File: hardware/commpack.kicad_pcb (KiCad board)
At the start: 2 copper layers, 103.8 x 62.5 mm, 15 parts, among them J1 1240COMM, J2 1240COMM_EXT, J3 L8BE-1G1T-91A, J4 USB_B, U3 27C128

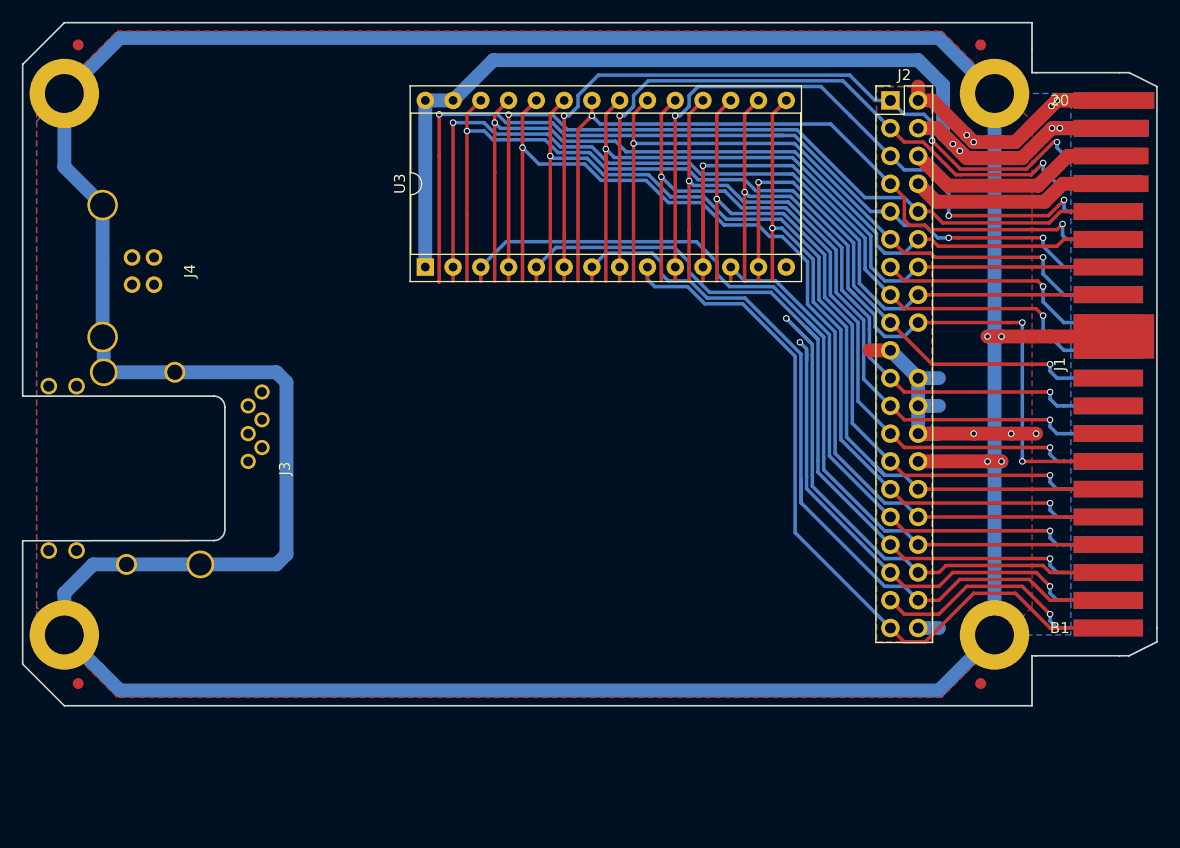
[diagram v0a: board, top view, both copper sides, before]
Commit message: Add Omega2 footprint to board.
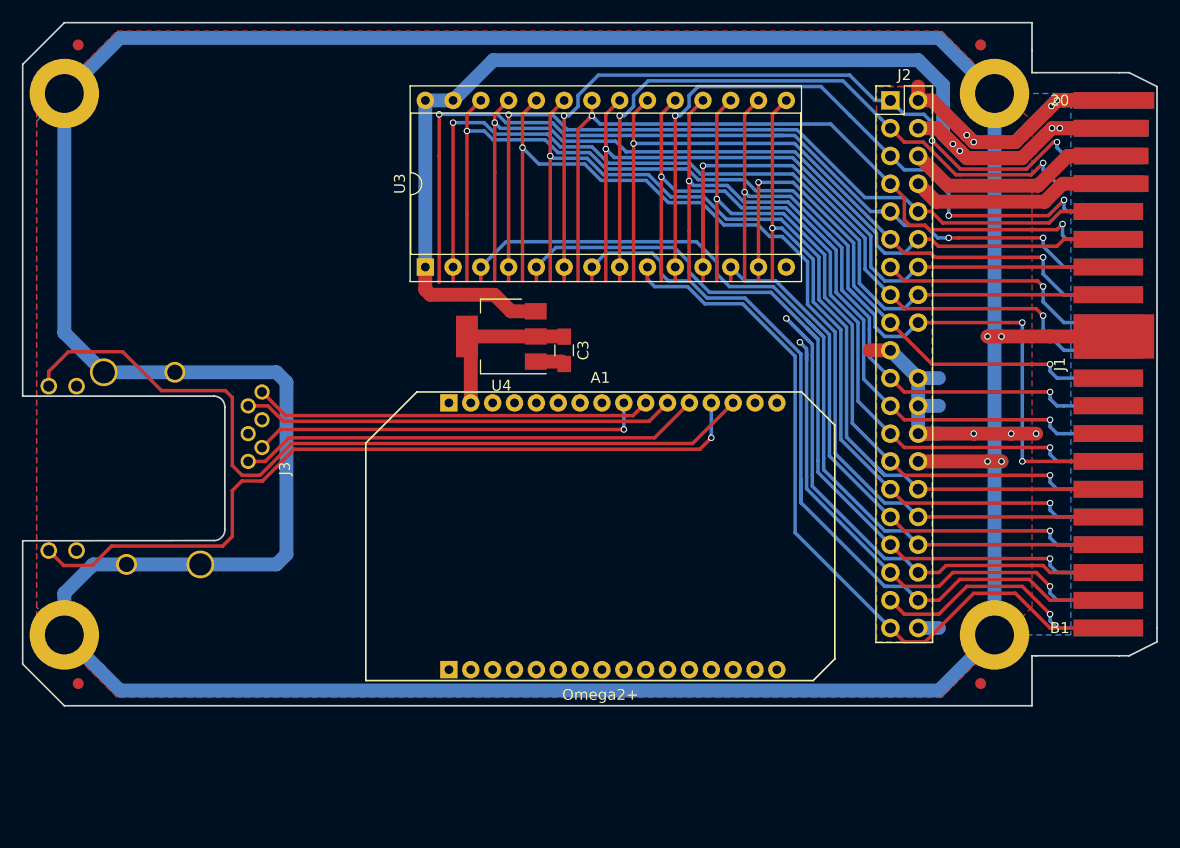
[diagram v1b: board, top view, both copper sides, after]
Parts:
- removed J4: USB_B, USB-B
- added A1: Omega2+, Omega2, F.Cu at (174.8, 104.6)
- added C3: 22u, Capacitors_SMD:C_0805_HandSoldering, F.Cu at (171.4, 87.6)
- added U4: AP1117-33, TO_SOT_Packages_SMD:SOT-223-3_TabPin2, F.Cu at (165.7, 86.4)
- moved Bonsai 16.6 mm to (186.7, 105.4)
- moved G*** 16.3 mm to (172.7, 104.1)
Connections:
- J3 pad 13: Net-(J3-Pad13) -> GND
- J3 pad 15: Net-(J3-Pad15) -> GND
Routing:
- net Net-(A1-PadB14): track 0.00 -> 75.8 mm
- net Net-(A1-PadB13): track 0.00 -> 71.7 mm, vias 0 -> 1
- net Net-(A1-PadB12): track 0.00 -> 42.6 mm
- net Net-(A1-PadB11): track 0.00 -> 39.6 mm
- net Net-(A1-PadB10): track 0.00 -> 36.5 mm
- net Net-(A1-PadB9): track 0.00 -> 36.2 mm, vias 0 -> 1
- net +3V3: track 0.00 -> 15.1 mm
- net +5V: track 96.2 -> 109.2 mm
- net GND: track 53.5 -> 56.2 mm

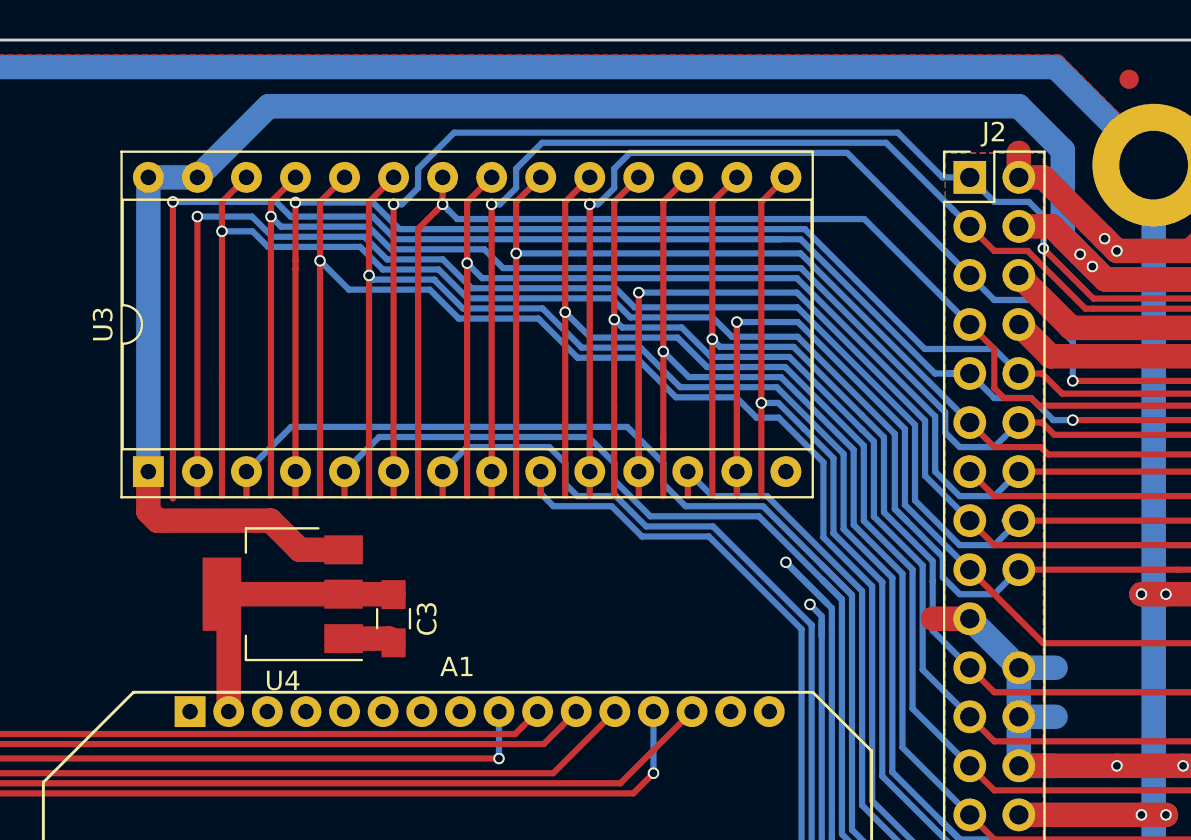
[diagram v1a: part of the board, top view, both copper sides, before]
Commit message: Reroute traces under 27C128 socket again.
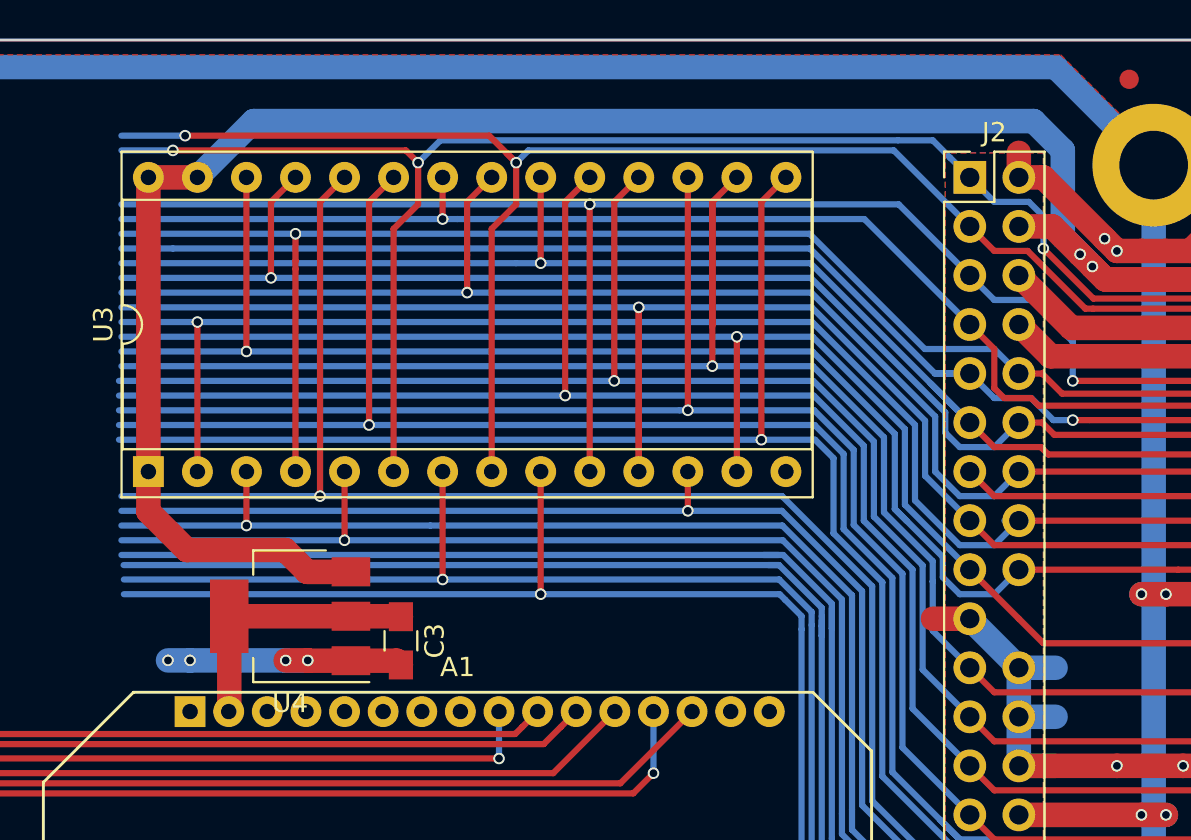
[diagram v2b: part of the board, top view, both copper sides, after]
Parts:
- moved C3 1.20 mm to (171.8, 88.8)
- moved U4 1.20 mm to (166.1, 87.5)
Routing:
- net /H-RST: track 44.5 -> 81.8 mm, vias 2 -> 1
- net /H-~CS: track 47.1 -> 80.6 mm, vias 1 -> 0
- net /H-D4: track 60.0 -> 89.6 mm
- net /H-D3: track 64.1 -> 93.6 mm
- net /H-D2: track 47.9 -> 77.5 mm
- net /H-D1: track 50.0 -> 79.3 mm, vias 1 -> 2
- net /H-D0: track 62.1 -> 86.6 mm
- net /H-A1: track 67.7 -> 91.5 mm, vias 0 -> 1
- net /H-D5: track 68.6 -> 90.6 mm
- net /H-A0: track 61.0 -> 81.2 mm
- net /H-A2: track 64.1 -> 83.8 mm, vias 2 -> 3
- net /H-D6: track 67.6 -> 86.0 mm
- net /H-A3: track 71.3 -> 88.5 mm, vias 0 -> 1
- net /H-D7: track 72.4 -> 88.5 mm
- net /H-INT: track 81.9 -> 67.9 mm, vias 3 -> 2
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
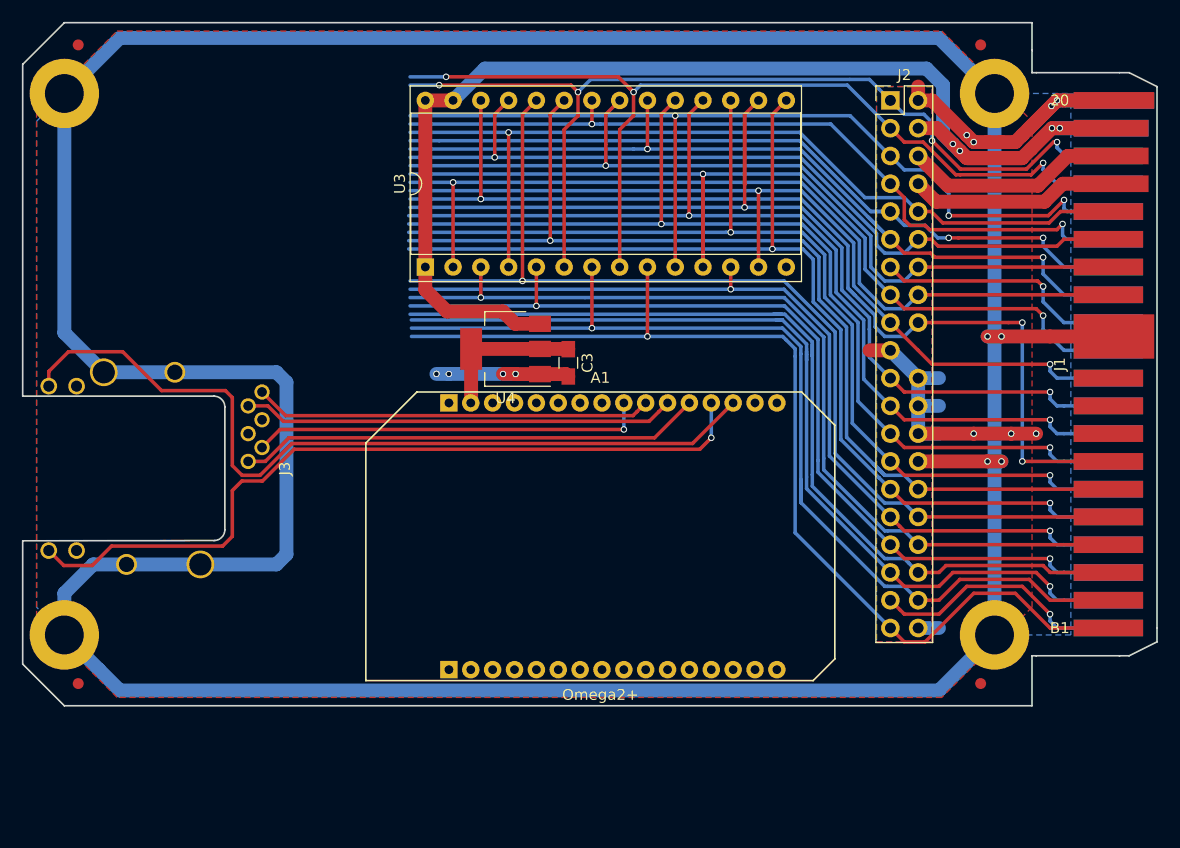
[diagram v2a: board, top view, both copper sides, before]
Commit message: Change ATA pinout, rip up EPROM socket and Omega2.
I missed two grounded pins when I did the original ATA connector pinout,
so this drops the +12V and -12V connections and rearranges everything to
avoid shorting two of the address lines to ground.
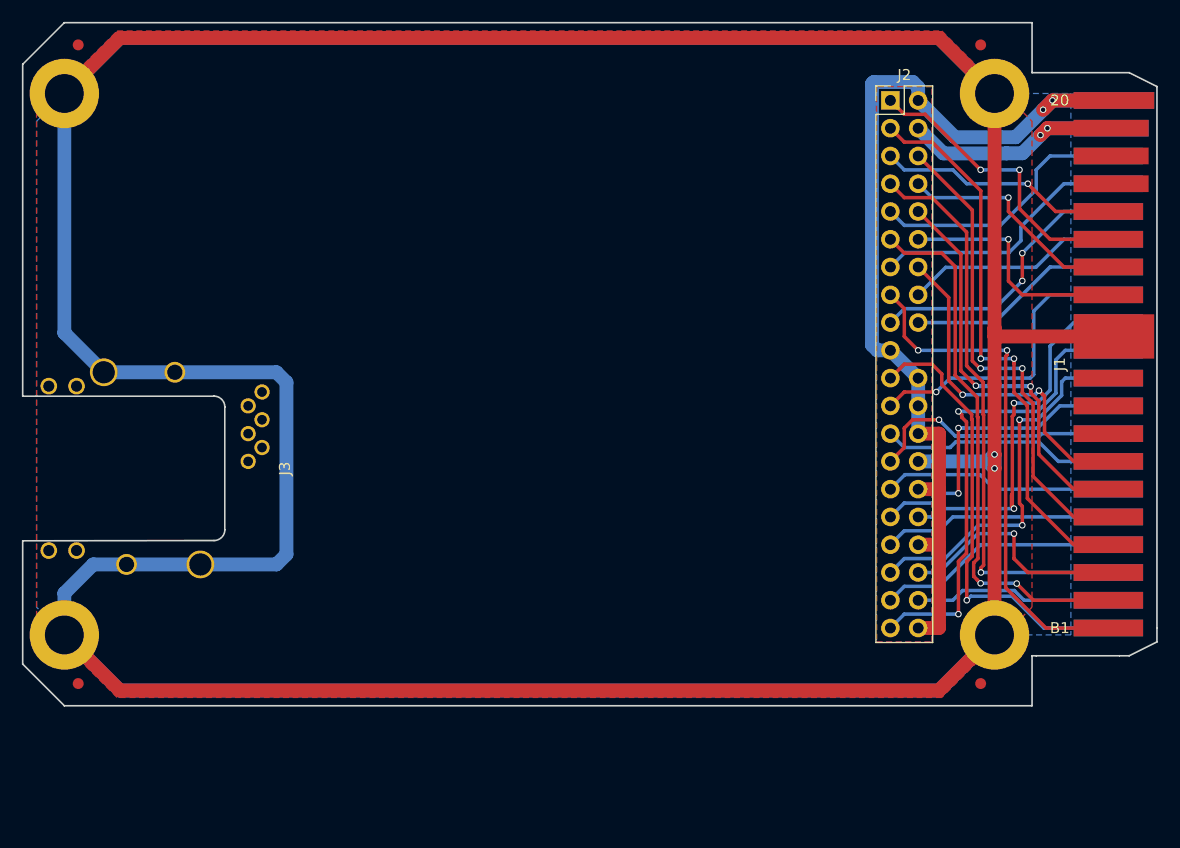
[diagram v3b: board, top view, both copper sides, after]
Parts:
- removed A1: Omega2+, Omega2
- removed Bonsai: Bonsai, ether1240:Bonsai
- removed C3: 22u, Capacitors_SMD:C_0805_HandSoldering
- removed G***: LOGO, ether1240:OSHW
- removed U3: 27C128, Housings_DIP:DIP-28_W15.24mm_Socket
- removed U4: AP1117-33, TO_SOT_Packages_SMD:SOT-223-3_TabPin2
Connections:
- J1 pad B17: +12VA -> Net-(J1-PadB17)
- J1 pad B18: -12VA -> Net-(J1-PadB18)
- J2 pad 1: /H-A4 -> /H-A8
- J2 pad 10: /H-A6 -> /H-A11
- J2 pad 11: /H-~RS -> /H-A3
- J2 pad 12: /H-A8 -> /H-A12
- J2 pad 13: Net-(J1-PadA12) -> /H-A2
- J2 pad 14: /H-A10 -> /H-A13
- J2 pad 15: /H-D0 -> /H-A1
- J2 pad 16: /H-A12 -> /H-~RD
- J2 pad 17: /H-D2 -> /H-A0
- J2 pad 18: /H-A13 -> /H-INT
- J2 pad 21: /H-D4 -> /H-~WR
- J2 pad 23: /H-D6 -> /H-~RS
- J2 pad 27: /H-D5 -> /H-D6
- J2 pad 29: /H-D3 -> /H-D5
- J2 pad 3: /H-A2 -> /H-A7
- J2 pad 30: /H-A11 -> GND
- J2 pad 31: /H-D1 -> /H-D4
- J2 pad 32: /H-A9 -> Net-(J1-PadA12)
- J2 pad 33: /H-A5 -> /H-D3
- J2 pad 34: /H-A7 -> GND
- J2 pad 35: /H-RST -> /H-D2
- J2 pad 37: /H-~WR -> /H-D1
- J2 pad 38: /H-A3 -> /H-RST
- J2 pad 39: /H-A1 -> /H-D0
- J2 pad 5: /H-A0 -> /H-A6
- J2 pad 6: -12VA -> /H-A9
- J2 pad 7: /H-~RD -> /H-A5
- J2 pad 8: +12VA -> /H-A10
- J2 pad 9: /H-INT -> /H-A4
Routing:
- net Earth_Protective: track 332.2 -> 510.2 mm, vias 4 -> 2
- net +5V: track 109.4 -> 19.4 mm, vias 4 -> 2
- net /H-D3: track 93.6 -> 17.8 mm, vias 2 -> 0
- net Net-(A1-PadB14): track 75.8 -> 0.00 mm
- net /H-D5: track 90.6 -> 17.9 mm, vias 2 -> 0
- net Net-(A1-PadB13): track 71.7 -> 0.00 mm, vias 1 -> 0
- net /H-D7: track 88.5 -> 18.2 mm, vias 2 -> 0
- net /H-RST: track 81.8 -> 15.0 mm, vias 1 -> 0
- net /H-D4: track 89.6 -> 24.5 mm
- net /H-A13: track 91.9 -> 28.3 mm, vias 3 -> 2
- net /H-D6: track 86.0 -> 22.4 mm, vias 2 -> 1
- net /H-A4: track 84.2 -> 21.0 mm, vias 4 -> 0
- net /H-A2: track 83.8 -> 20.7 mm, vias 3 -> 0
- net /H-~CS: track 80.6 -> 18.5 mm, vias 0 -> 1
- net /H-D1: track 79.3 -> 18.9 mm, vias 2 -> 0
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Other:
- outline, holes or cut-outs redrawn
- board text removed: "+12"
- board text removed: "-12"

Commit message: Clean up routing from card edge to ATA connector.
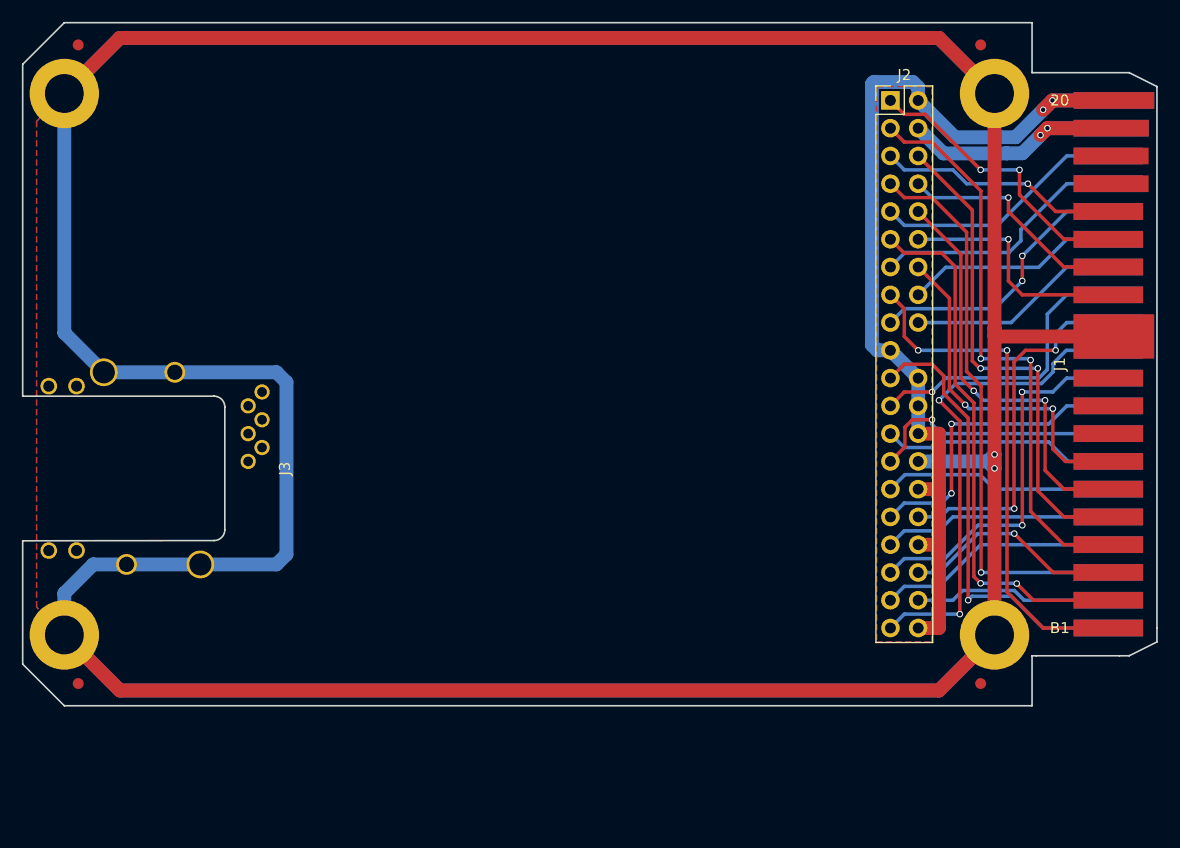
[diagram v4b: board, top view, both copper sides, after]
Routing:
- net /H-A11: track 39.1 -> 35.1 mm
- net /H-D6: track 22.4 -> 20.2 mm
- net /H-A9: track 41.2 -> 42.5 mm
- net /H-~CS: track 18.5 -> 17.2 mm
- net /H-A7: track 48.3 -> 49.6 mm
- net /H-D0: track 40.5 -> 41.9 mm
- net /H-A4: track 21.0 -> 19.9 mm
- net /H-A8: track 24.1 -> 23.4 mm
- net Net-(J1-PadA12): track 31.1 -> 30.4 mm
